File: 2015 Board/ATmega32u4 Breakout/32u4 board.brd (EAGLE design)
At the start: 21.2 x 40.8 mm, 17 parts, among them X1 MINI-USB-UX60A-MB-5ST

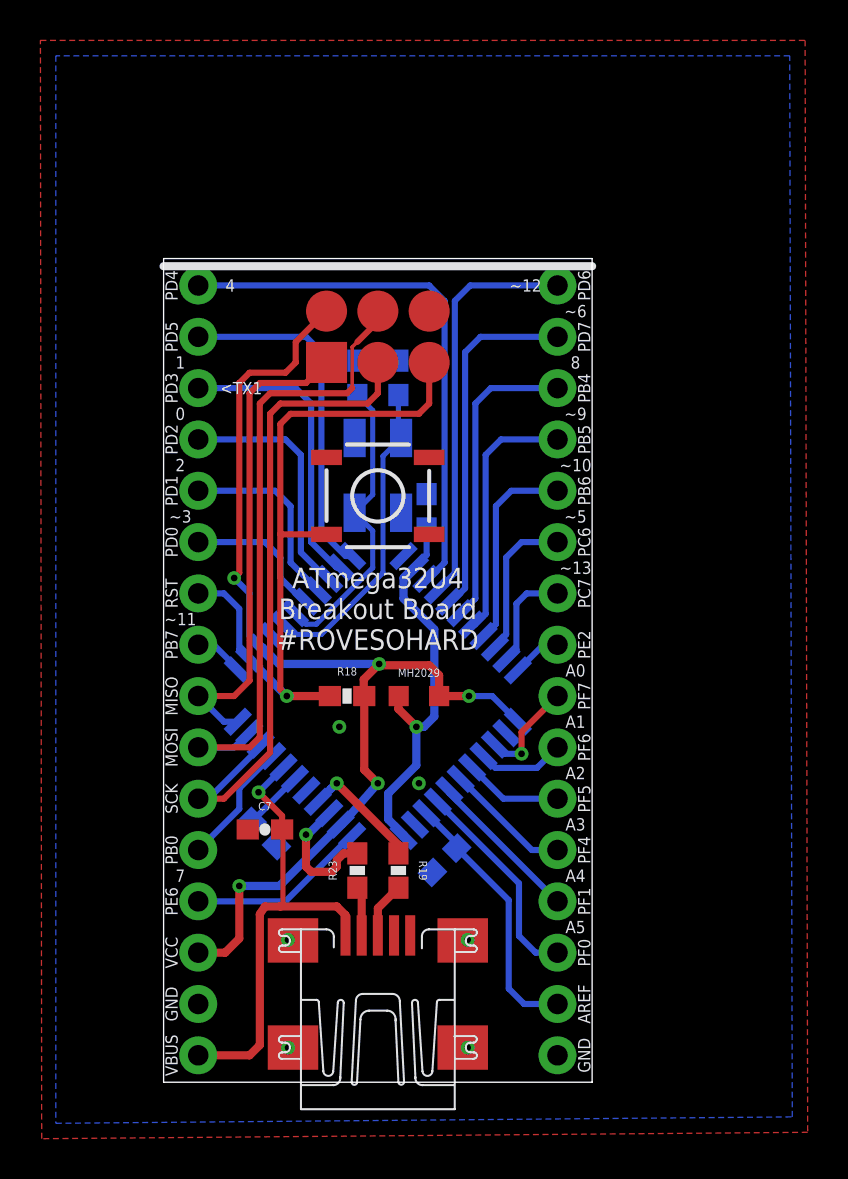
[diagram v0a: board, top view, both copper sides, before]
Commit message: More cleanup on the breakout board
Did more cleanup because I have a problem
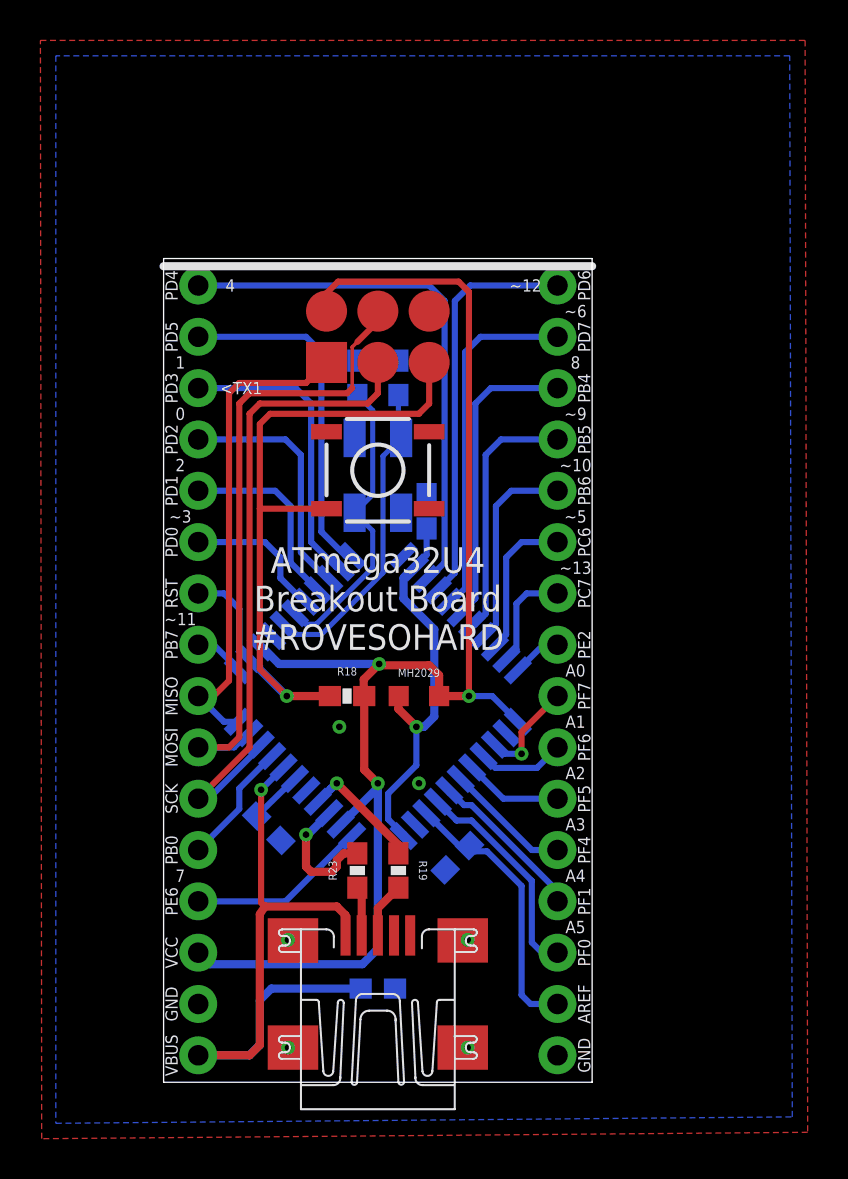
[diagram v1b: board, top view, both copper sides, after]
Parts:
- moved C7 9.66 mm to (10.6, 4.64), flipped to the bottom
- moved S1 1.27 mm to (10.6, 30.3)
- moved C21 0.65 mm to (14.5, 11.1)
- moved C6 0.35 mm to (5.21, 12.6)
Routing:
- net VCC: track 55.6 -> 70.4 mm, vias 5 -> 3
- net VBUS: track 23.3 -> 33.5 mm
- net RST: track 35.5 -> 38.0 mm
- net AREF: track 13.1 -> 13.8 mm

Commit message: Finished Symmetry
Everything is as symmetric as I can get it
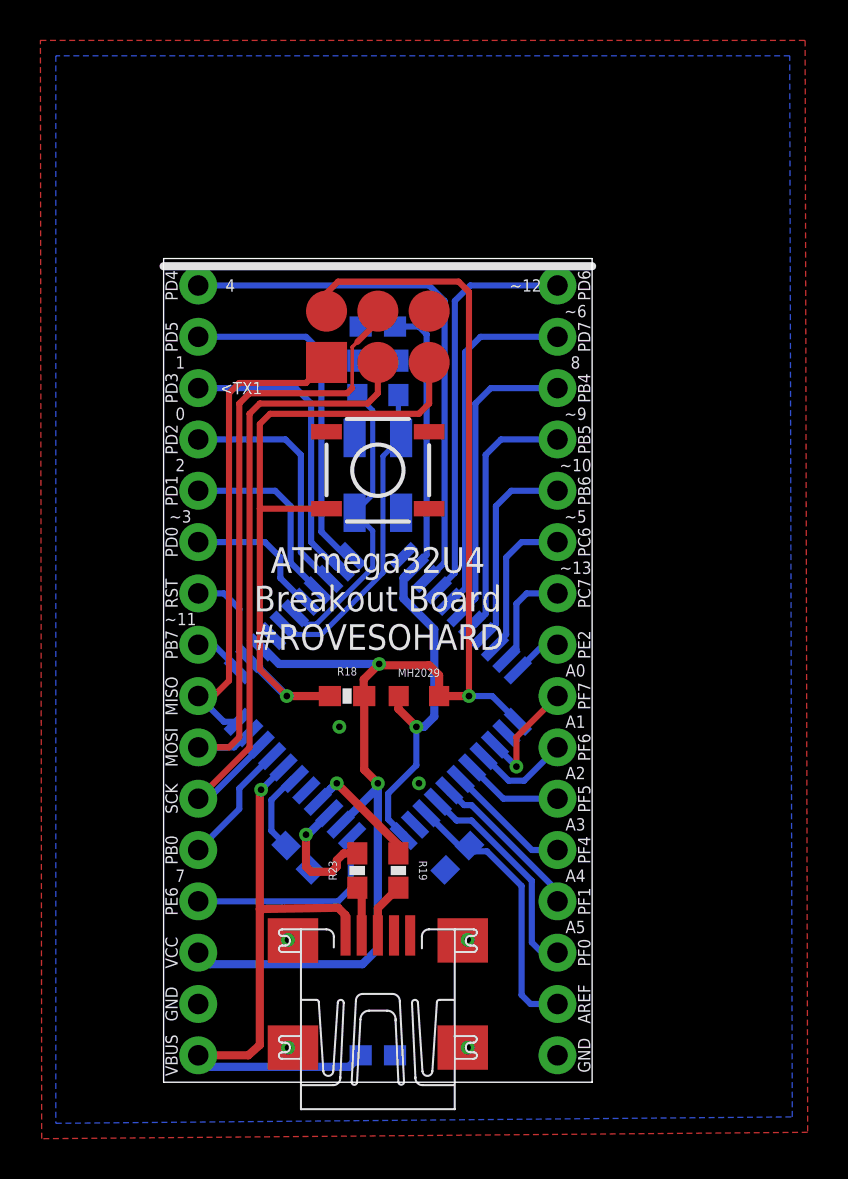
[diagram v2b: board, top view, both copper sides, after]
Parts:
- moved C20 9.46 mm to (10.6, 37.4), turned to 0 degrees
- moved C7 3.30 mm to (10.6, 1.33)
- moved C6 2.07 mm to (6.67, 11.1)
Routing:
- net N$31: track 19.7 -> 31.1 mm
- net VBUS: track 33.5 -> 31.4 mm
- net PE6: track 8.96 -> 10.5 mm
- net N$27: track 2.65 -> 4.16 mm
- net PF7: track 5.11 -> 5.86 mm
- net PF6: track 4.32 -> 4.85 mm

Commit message: Finished and ready for fab
I think unless anyone finds any little thing to change
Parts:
- moved C7 2.86 mm to (10.6, 4.19), turned to 90 degrees
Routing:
- net VBUS: track 31.4 -> 34.1 mm
- net PB0: track 6.18 -> 7.33 mm
- net SCK: track 32.7 -> 33.7 mm
- net PF7: track 5.86 -> 6.75 mm

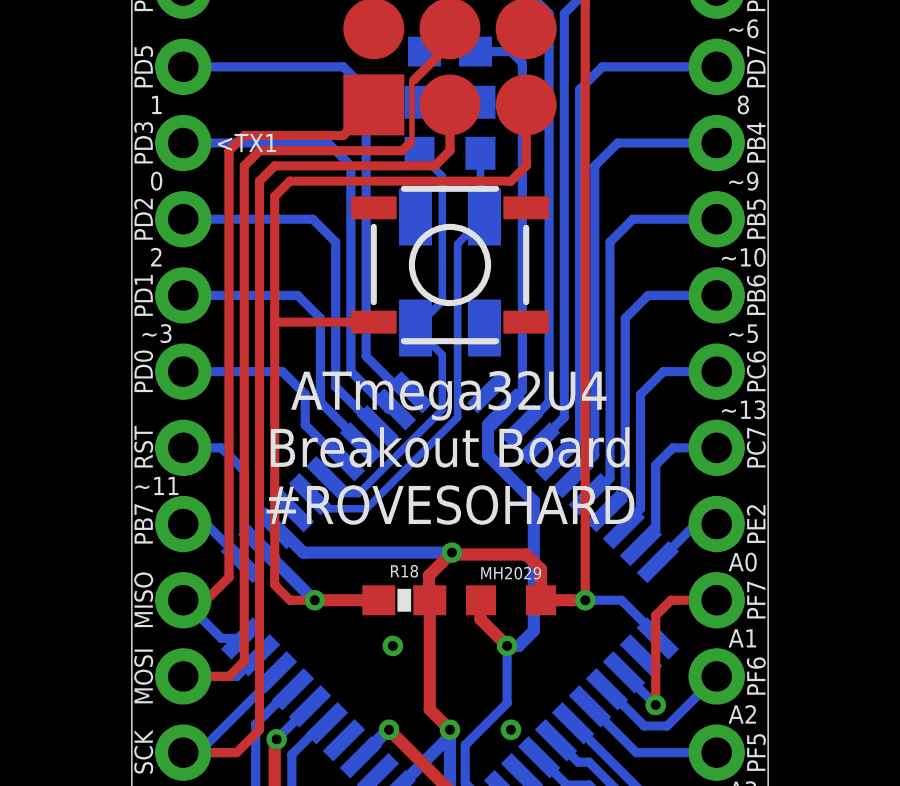
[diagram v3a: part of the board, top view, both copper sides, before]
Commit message: Added an LED for Nathan
Since none of our boards have indicator lights on it he said it would
be nice and I agreed.  So I added an LED off of VCC to show when the
board is on.
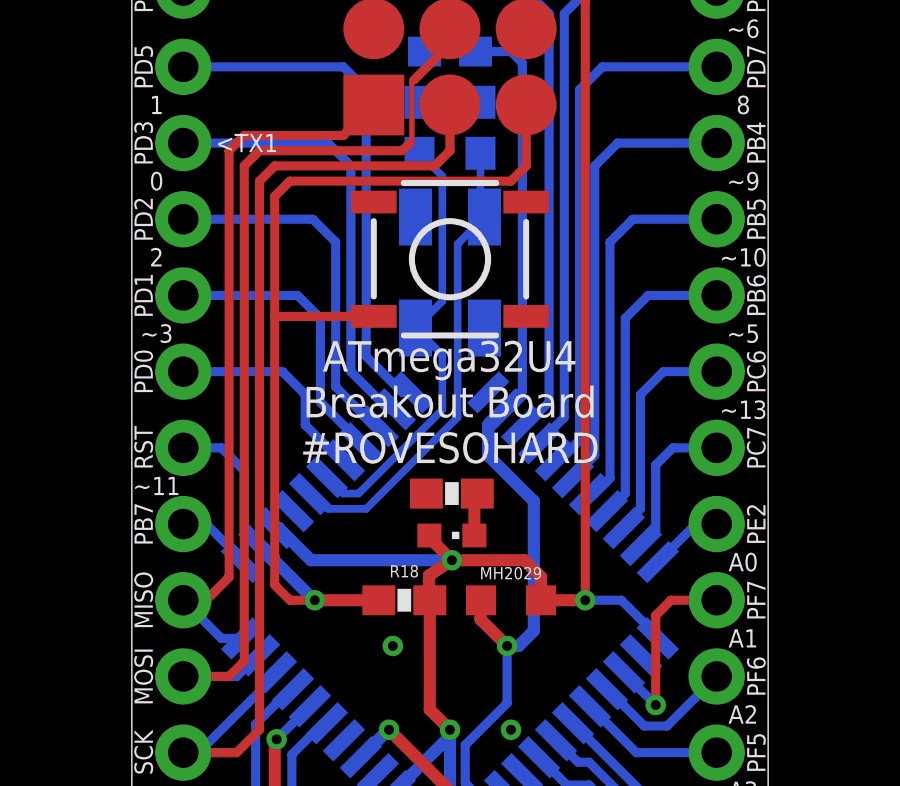
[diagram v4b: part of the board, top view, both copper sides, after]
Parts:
- added LED1: (no value), adafruit:CHIPLED_0603
- added R1: (no value), SparkFun-Resistors:0603-RES
- moved S1 0.19 mm to (10.6, 30.5)
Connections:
- new net N$1: LED1.C, R1.2
- net GND: now also R1.1
- net VCC: now also LED1.A
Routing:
- net N$1: track 0.00 -> 1.44 mm
- net VCC: track 70.4 -> 71.2 mm
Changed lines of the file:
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@@
 <dimension x1="1.7145" y1="1.3335" x2="19.4945" y2="1.3335" x3="10.6045" y3="-3.7465" textsize="1.778" layer="27" dtype="vertical" unit="mil" visible="yes"/>
 <dimension x1="21.5265" y1="40.767" x2="21.5265" y2="0" x3="24.0665" y3="20.3835" textsize="1.778" layer="27" dtype="vertical" unit="mil" visible="yes"/>
-<text x="10.6045" y="24.1935" size="1.27" layer="25" font="vector" align="center">ATmega32U4
+<text x="10.6045" y="25.7175" size="1.016" layer="25" font="vector" align="center">ATmega32U4
 Breakout Board
 #ROVESOHARD</text>
@@
 <attribute name="OC_FARNELL" value="unknown" x="10.6045" y="5.0165" size="1.778" layer="27" rot="R90" display="off"/>
 </element>
-<element name="S1" library="SparkFun-Electromechanical" package="TACTILE_SWITCH_SMD" value="SWITCH-MOMENTARY-2SMD" x="10.6045" y="30.2895" smashed="yes"/>
+<element name="S1" library="SparkFun-Electromechanical" package="TACTILE_SWITCH_SMD" value="SWITCH-MOMENTARY-2SMD" x="10.6045" y="30.48" smashed="yes"/>
 <element name="C18" library="SparkFun-Capacitors" package="0603-CAP" value="0.1uF" x="11.6205" y="34.8615" smashed="yes" rot="MR90">
 <attribute name="PROD_ID" value="CAP-00810" x="17.2085" y="34.8615" size="1.778" layer="28" rot="MR90" display="off"/>
@@
 </element>
 <element name="U$4" library="SparkFun-FreqCtrl" package="CRYSTAL-SMD-5X3" value="CRYSTAL-GROUNDED" x="10.6045" y="30.0355" smashed="yes" rot="MR270"/>
+<element name="LED1" library="adafruit" package="CHIPLED_0603" value="" x="10.668" y="21.2725" smashed="yes" rot="R270">
+<attribute name="VALUE" x="9.398" y="19.3675" size="1.27" layer="27"/>
+</element>
+<element name="R1" library="SparkFun-Resistors" package="0603-RES" value="" x="10.668" y="22.6695" smashed="yes">
+<attribute name="VALUE" x="9.652" y="21.5265" size="0.4064" layer="27" font="vector"/>
+</element>
 </elements>
 <signals>
@@
 <contactref element="U$4" pad="2"/>
 <contactref element="U$4" pad="4"/>
+<contactref element="R1" pad="1"/>
 </signal>
 <signal name="D+">
@@
 <wire x1="12.6365" y1="33.0835" x2="5.2705" y2="33.0835" width="0.3048" layer="1"/>
 <wire x1="5.2705" y1="33.0835" x2="4.7625" y2="32.5755" width="0.3048" layer="1"/>
-<wire x1="4.7625" y1="32.5755" x2="4.7625" y2="28.3845" width="0.3048" layer="1"/>
-<wire x1="4.7625" y1="28.3845" x2="4.7625" y2="19.6215" width="0.3048" layer="1"/>
+<wire x1="4.7625" y1="32.5755" x2="4.7625" y2="28.575" width="0.3048" layer="1"/>
+<wire x1="4.7625" y1="28.575" x2="4.7625" y2="19.6215" width="0.3048" layer="1"/>
 <contactref element="S1" pad="3"/>
-<wire x1="8.0645" y1="28.3845" x2="4.7625" y2="28.3845" width="0.3048" layer="1"/>
+<wire x1="8.0645" y1="28.575" x2="4.7625" y2="28.575" width="0.3048" layer="1"/>
 <wire x1="4.7625" y1="19.6215" x2="5.2705" y2="19.1135" width="0.3048" layer="1"/>
 <wire x1="5.2705" y1="19.1135" x2="6.096" y2="19.1135" width="0.3048" layer="1"/>
@@
 <wire x1="15.113" y1="19.1135" x2="13.6365" y2="19.1135" width="0.4064" layer="1"/>
 <wire x1="4.806225" y1="21.5176625" x2="4.8983375" y2="21.5176625" width="0.4064" layer="16"/>
-<wire x1="4.8983375" y1="21.5176625" x2="5.715" y2="20.701" width="0.4064" layer="16"/>
-<wire x1="5.715" y1="20.701" x2="10.668" y2="20.701" width="0.4064" layer="16"/>
-<via x="10.668" y="20.701" extent="1-16" drill="0.3302"/>
+<wire x1="4.8983375" y1="21.5176625" x2="5.969" y2="20.447" width="0.4064" layer="16"/>
+<wire x1="5.969" y1="20.447" x2="10.668" y2="20.447" width="0.4064" layer="16"/>
+<via x="10.668" y="20.447" extent="1-16" drill="0.3302"/>
 <wire x1="9.906" y1="19.138" x2="9.9305" y2="19.1135" width="0.4064" layer="1"/>
 <wire x1="9.906" y1="19.138" x2="9.906" y2="19.939" width="0.4064" layer="1"/>
-<wire x1="9.906" y1="19.939" x2="10.668" y2="20.701" width="0.4064" layer="1"/>
-<wire x1="13.6365" y1="19.1135" x2="13.6365" y2="20.1455" width="0.4064" layer="1"/>
-<wire x1="13.6365" y1="20.1455" x2="13.1445" y2="20.6375" width="0.4064" layer="1"/>
-<wire x1="13.1445" y1="20.6375" x2="10.7315" y2="20.6375" width="0.4064" layer="1"/>
-<wire x1="10.7315" y1="20.6375" x2="10.668" y2="20.701" width="0.4064" layer="1"/>
+<wire x1="9.906" y1="19.939" x2="10.668" y2="20.447" width="0.4064" layer="1"/>
+<wire x1="13.6365" y1="19.1135" x2="13.6365" y2="19.8915" width="0.4064" layer="1"/>
 <wire x1="9.9305" y1="19.1135" x2="9.9305" y2="15.4695" width="0.4064" layer="1"/>
 <wire x1="9.9305" y1="15.4695" x2="10.6045" y2="14.7955" width="0.4064" layer="1"/>
@@
 <wire x1="17.534146875" y1="17.898853125" x2="16.3195" y2="19.1135" width="0.3048" layer="16"/>
 <wire x1="16.3195" y1="19.1135" x2="15.113" y2="19.1135" width="0.3048" layer="16"/>
+<contactref element="LED1" pad="A"/>
+<wire x1="9.918" y1="21.2725" x2="9.918" y2="21.197" width="0.4064" layer="1"/>
+<wire x1="10.668" y1="20.447" x2="13.081" y2="20.447" width="0.4064" layer="1"/>
+<wire x1="13.081" y1="20.447" x2="13.6365" y2="19.8915" width="0.4064" layer="1"/>
+<wire x1="9.918" y1="21.197" x2="10.668" y2="20.447" width="0.4064" layer="1"/>
 </signal>
 <signal name="PF7">
@@
 <wire x1="11.6205" y1="31.7655" x2="11.7545" y2="31.8855" width="0.254" layer="16"/>
 </signal>
+<signal name="N$1">
+<contactref element="LED1" pad="C"/>
+<contactref element="R1" pad="2"/>
+<wire x1="11.418" y1="21.2725" x2="11.418" y2="22.5695" width="0.4064" layer="1"/>
+<wire x1="11.418" y1="22.5695" x2="11.518" y2="22.6695" width="0.4064" layer="1"/>
+</signal>
 </signals>
